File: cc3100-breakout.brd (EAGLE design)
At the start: 46 x 48.5 mm, 56 parts, among them IC4 CC3100, IC5 S25FL216K0PMFI011, X4 DNP - ABS07-32.768KHZ-T, X5 Q24FA20H00396, X6 MC-921

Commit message: some more routing
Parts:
- moved C64 4.58 mm to (23.9, 13.1), turned to 0 degrees
- moved C49 0.28 mm to (23.8, 17.8)
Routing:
- net N$17: track 19.5 -> 21.9 mm, vias 5 -> 8
- net N$18: track 16.9 -> 15.7 mm, vias 1 -> 2
- net GND: track 48.2 -> 47.1 mm, vias 30 -> 29
- added copper zone on layer 1, net +3V3
- added copper zone on layer 2, net +3V3
- added copper zone on layer 15, net GND
- added copper zone on layer 2, net N$17
- added copper zone on layer 2, net N$18

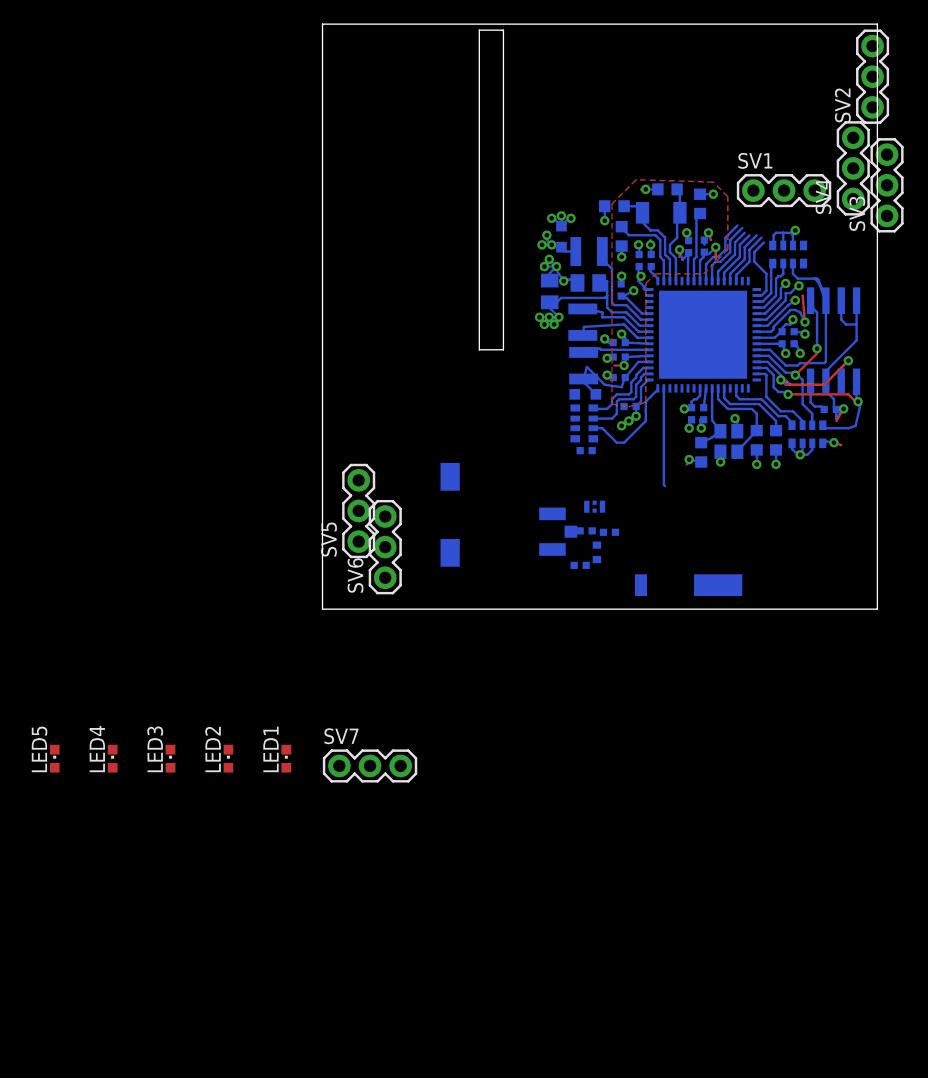
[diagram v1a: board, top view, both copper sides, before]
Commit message: started to rework pin mapping a little so the lcd uses the FSMC pins
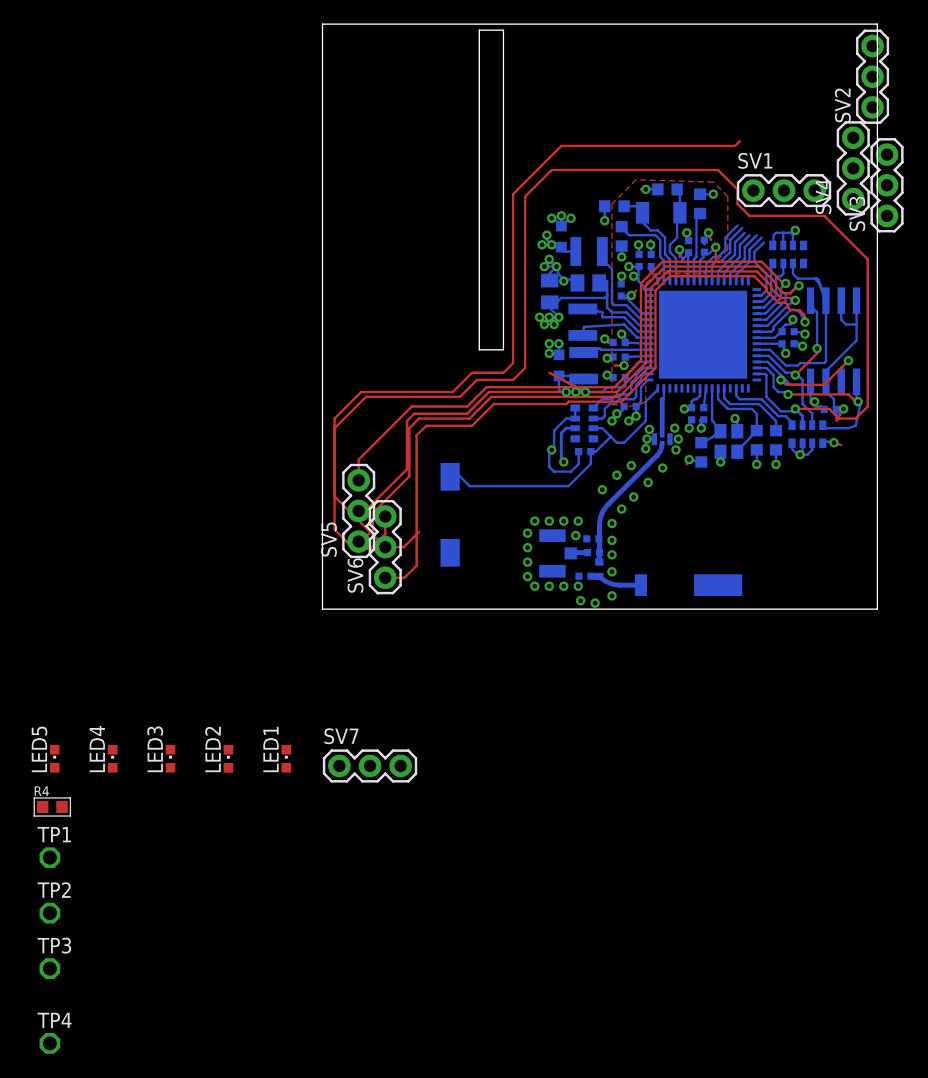
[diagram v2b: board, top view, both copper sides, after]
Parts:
- added R4: 150, passives-7351:R0603-N
- added TP1, TP2, TP3, TP4: TPPAD1-11, TiLDA Mk3 Parts:P1-11
- moved FL1 7.92 mm to (30.2, 14.1)
- moved C49 3.24 mm to (21.6, 20.2), turned to 270 degrees
- moved R41 1.90 mm to (24.5, 4.69)
- moved X6 1.80 mm to (21.1, 4.62)
- moved C67 1.48 mm to (24.4, 5.83), turned to 0 degrees
- moved L7 1.41 mm to (24.9, 3.31)
- moved C70 0.98 mm to (23.8, 2.73)
- moved C64 0.14 mm to (23.7, 13.1), turned to 180 degrees
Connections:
- new net N$14: LED1.C, R4.2
- net +3V3: now also LED1.A
- net GND: now also R4.1, TP4.TP
- net N$17: now also TP2.TP
- net N$18: now also TP1.TP
- net N$22: now also TP3.TP
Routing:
- net WIFI_INTR: track 6.82 -> 106.2 mm, vias 0 -> 1
- net WIFI_!HIB: track 5.71 -> 73.1 mm
- net SPI1_NSS: track 7.61 -> 62.7 mm
- net SPI1_MISO: track 4.43 -> 57.9 mm
- net SPI1_MOSI: track 5.23 -> 57.5 mm
- net SPI1_SCK: track 3.90 -> 52.3 mm
- net WIFI_!RESET: track 8.71 -> 24.8 mm
- net N$2: track 0.00 -> 12.9 mm
- net GND: track 47.1 -> 59.7 mm, vias 29 -> 69
- net N$18: track 15.7 -> 25.1 mm, vias 2 -> 6
- net ANT: track 0.00 -> 4.29 mm
- net N$3: track 8.14 -> 3.94 mm
- net +3V3: track 37.9 -> 41.8 mm, vias 8 -> 9
- net N$17: track 21.9 -> 20.3 mm, vias 8 -> 7
- net N$48: track 0.00 -> 1.39 mm
- added copper zone on layer 2, net GND
- added copper zone on layer 2, net N$22
